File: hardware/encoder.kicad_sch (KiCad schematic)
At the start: 3 parts

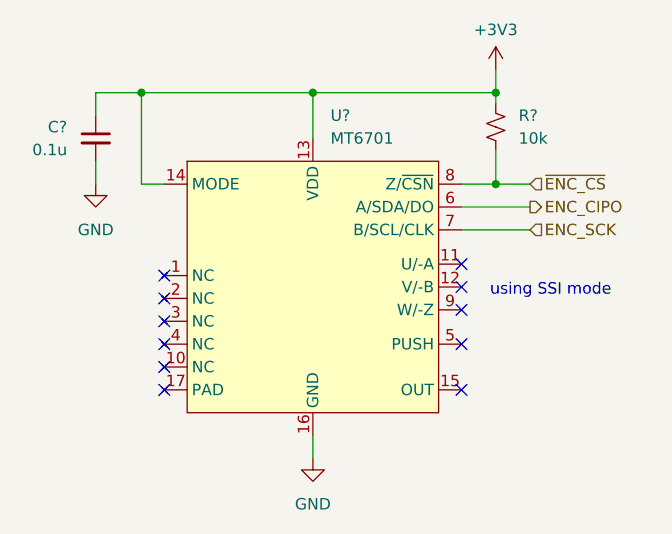
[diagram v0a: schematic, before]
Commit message: update schematic (Vref+ tie to Vdd) and go through ERC check
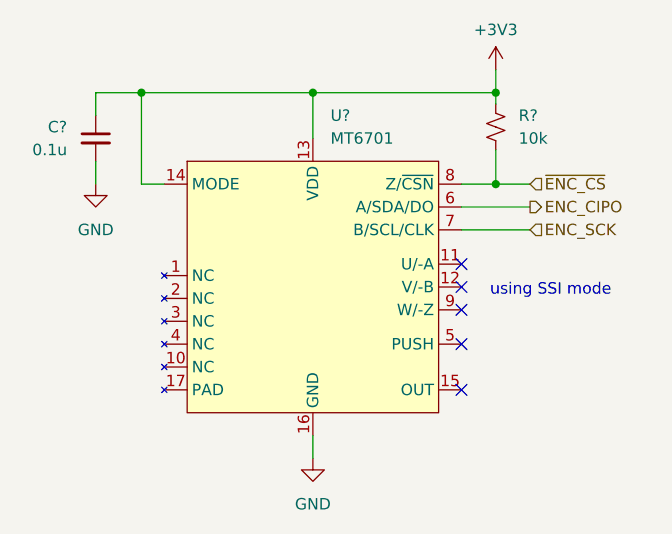
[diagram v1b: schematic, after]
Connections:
- no-connect marks 11 -> 5
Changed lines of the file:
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@@
   (no_connect (at 170.18 99.06))
   (no_connect (at 170.18 90.17))
-  (no_connect (at 137.16 93.98))
-  (no_connect (at 137.16 91.44))
-  (no_connect (at 137.16 96.52))
-  (no_connect (at 137.16 101.6))
   (no_connect (at 170.18 92.71))
   (no_connect (at 170.18 104.14))
-  (no_connect (at 137.16 99.06))
   (no_connect (at 170.18 95.25))
-  (no_connect (at 137.16 104.14))
   (wire (pts (xy 173.99 81.28) (xy 173.99 77.47))
     (stroke (width 0) (type default))
@@
       (effects (font (size 1.27 1.27)) hide)
     )
-    (pin "1")
+    (pin "2")
+    (pin "3")
+    (pin "4")
+    (pin "1")
+    (pin "10")
+    (pin "11")
+    (pin "12")
     (pin "13")
     (pin "14")
     (pin "15")
     (pin "16")
-    (pin "2")
-    (pin "3")
-    (pin "4")
+    (pin "17")
     (pin "5")
     (pin "6")
     (pin "7")
-    (pin "10")
-    (pin "11")
-    (pin "12")
-    (pin "17")
     (pin "8")
     (pin "9")
